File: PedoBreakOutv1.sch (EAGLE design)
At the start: 18 parts, among them IC1 LM1117MPX-2.85, J1 1050170001, J2 POWER_JACKSLT, J3 AVR_SPI_PROG_3X2NS, U1 ATTINY85-20P

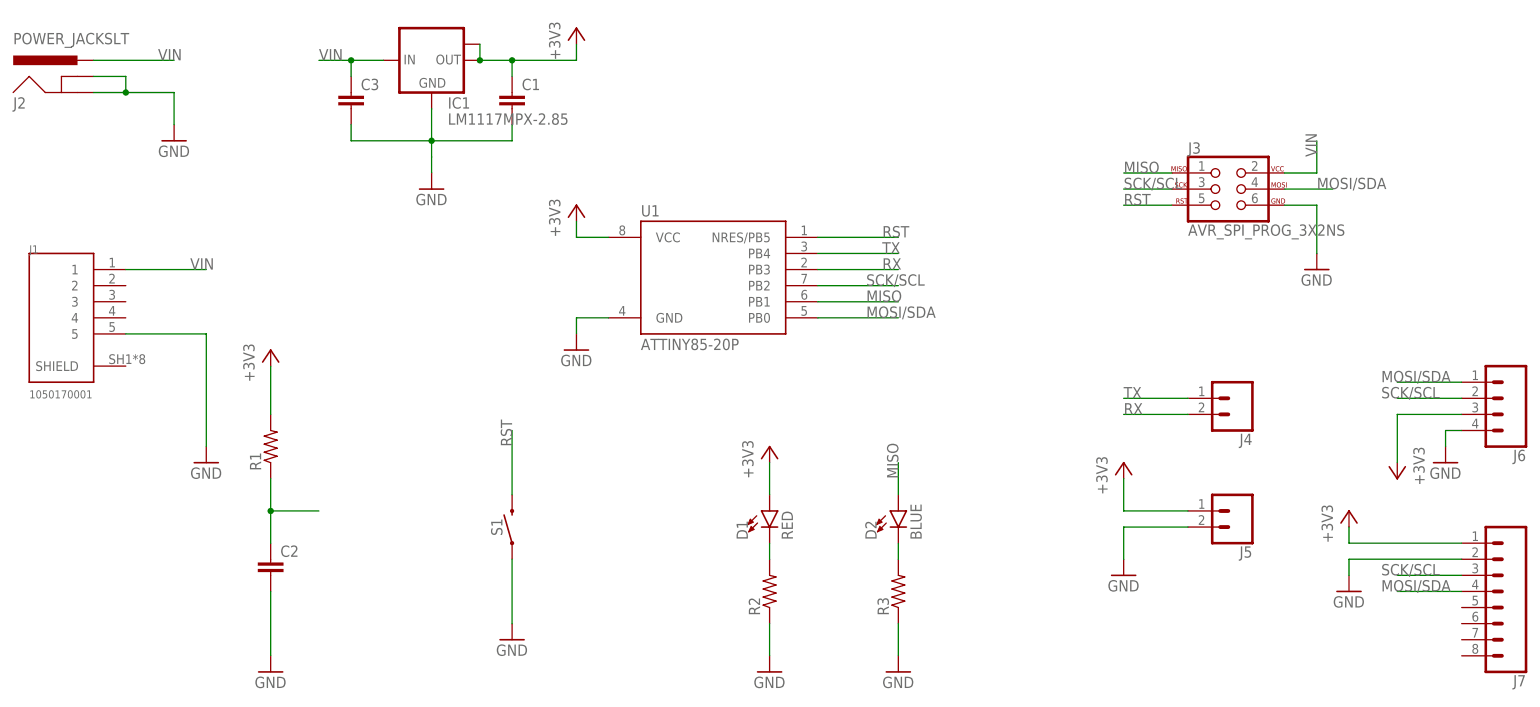
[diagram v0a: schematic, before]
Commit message: Reduced size of board, removed ground plane issues
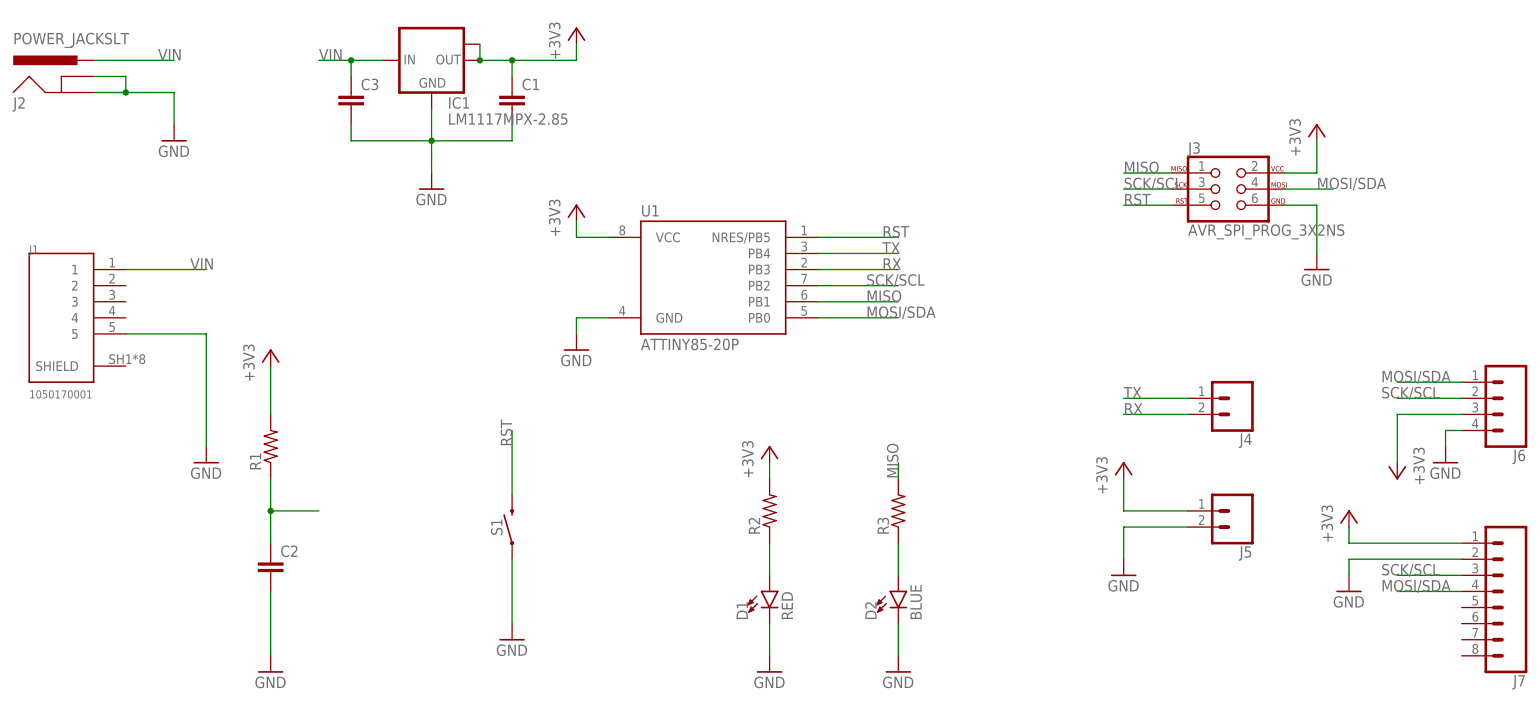
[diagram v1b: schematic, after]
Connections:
- net +3V3: now also J3.2, R2.2; no longer D1.A
- net GND: now also D1.C, D2.C; no longer R2.1, R3.1
- net MISO: now also R3.2; no longer D2.A
- net N$1: now also D1.A, R2.1; no longer D1.C, R2.2
- net N$3: now also D2.A, R3.1; no longer D2.C, R3.2
- net VIN: no longer J3.2
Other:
- moved on the sheet: D1, D2, R2, R3
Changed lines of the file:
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@@
 <?xml version="1.0" encoding="utf-8"?>
 <!DOCTYPE eagle SYSTEM "eagle.dtd">
-<eagle version="9.4.2">
+<eagle version="9.5.2">
 <drawing>
 <settings>
@@
 <part name="GND12" library="supply1" library_urn="urn:adsk.eagle:library:371" deviceset="GND" device=""/>
 <part name="IC1" library="lm1117" deviceset="LM1117MPX-*" device="" technology="2.85"/>
+<part name="+3V8" library="supply1" library_urn="urn:adsk.eagle:library:371" deviceset="+3V3" device=""/>
 </parts>
 <sheets>
@@
 <attribute name="VALUE" x="55.88" y="38.1" size="1.778" layer="96"/>
 </instance>
-<instance part="D1" gate="G$1" x="137.16" y="66.04" smashed="yes">
-<attribute name="NAME" x="133.731" y="61.468" size="1.778" layer="95" font="vector" rot="R90"/>
-<attribute name="VALUE" x="139.065" y="61.468" size="1.778" layer="96" font="vector" rot="R90" align="top-left"/>
-</instance>
-<instance part="D2" gate="G$1" x="157.48" y="66.04" smashed="yes">
-<attribute name="NAME" x="154.051" y="61.468" size="1.778" layer="95" font="vector" rot="R90"/>
-<attribute name="VALUE" x="159.385" y="61.468" size="1.778" layer="96" font="vector" rot="R90" align="top-left"/>
-</instance>
-<instance part="R2" gate="G$1" x="137.16" y="53.34" smashed="yes" rot="R90">
-<attribute name="NAME" x="135.6614" y="49.53" size="1.778" layer="95" rot="R90"/>
-<attribute name="VALUE" x="140.462" y="49.53" size="1.778" layer="96" rot="R90"/>
-</instance>
-<instance part="R3" gate="G$1" x="157.48" y="53.34" smashed="yes" rot="R90">
-<attribute name="NAME" x="155.9814" y="49.53" size="1.778" layer="95" rot="R90"/>
-<attribute name="VALUE" x="160.782" y="49.53" size="1.778" layer="96" rot="R90"/>
+<instance part="D1" gate="G$1" x="137.16" y="53.34" smashed="yes">
+<attribute name="NAME" x="133.731" y="48.768" size="1.778" layer="95" font="vector" rot="R90"/>
+<attribute name="VALUE" x="139.065" y="48.768" size="1.778" layer="96" font="vector" rot="R90" align="top-left"/>
+</instance>
+<instance part="D2" gate="G$1" x="157.48" y="53.34" smashed="yes">
+<attribute name="NAME" x="154.051" y="48.768" size="1.778" layer="95" font="vector" rot="R90"/>
+<attribute name="VALUE" x="159.385" y="48.768" size="1.778" layer="96" font="vector" rot="R90" align="top-left"/>
+</instance>
+<instance part="R2" gate="G$1" x="137.16" y="66.04" smashed="yes" rot="R90">
+<attribute name="NAME" x="135.6614" y="62.23" size="1.778" layer="95" rot="R90"/>
+<attribute name="VALUE" x="140.462" y="62.23" size="1.778" layer="96" rot="R90"/>
+</instance>
+<instance part="R3" gate="G$1" x="157.48" y="66.04" smashed="yes" rot="R90">
+<attribute name="NAME" x="155.9814" y="62.23" size="1.778" layer="95" rot="R90"/>
+<attribute name="VALUE" x="160.782" y="62.23" size="1.778" layer="96" rot="R90"/>
 </instance>
 <instance part="GND7" gate="1" x="137.16" y="40.64" smashed="yes">
@@
 <attribute name="NAME" x="86.36" y="129.54" size="1.778" layer="95"/>
 <attribute name="VALUE" x="86.36" y="127" size="1.778" layer="96"/>
+</instance>
+<instance part="+3V8" gate="G$1" x="223.52" y="127" smashed="yes">
+<attribute name="VALUE" x="220.98" y="121.92" size="1.778" layer="96" rot="R90"/>
 </instance>
 </instances>
@@
 </segment>
 <segment>
-<pinref part="R2" gate="G$1" pin="1"/>
-<pinref part="GND7" gate="1" pin="GND"/>
-<wire x1="137.16" y1="48.26" x2="137.16" y2="43.18" width="0.1524" layer="91"/>
-</segment>
-<segment>
-<pinref part="R3" gate="G$1" pin="1"/>
-<pinref part="GND8" gate="1" pin="GND"/>
-<wire x1="157.48" y1="48.26" x2="157.48" y2="43.18" width="0.1524" layer="91"/>
-</segment>
-<segment>
 <pinref part="J3" gate="G$1" pin="6"/>
 <wire x1="218.44" y1="114.3" x2="223.52" y2="114.3" width="0.1524" layer="91"/>
@@
 <pinref part="GND12" gate="1" pin="GND"/>
 <wire x1="228.6" y1="58.42" x2="228.6" y2="55.88" width="0.1524" layer="91"/>
+</segment>
+<segment>
+<pinref part="D1" gate="G$1" pin="C"/>
+<pinref part="GND7" gate="1" pin="GND"/>
+<wire x1="137.16" y1="48.26" x2="137.16" y2="43.18" width="0.1524" layer="91"/>
+</segment>
+<segment>
+<pinref part="D2" gate="G$1" pin="C"/>
+<pinref part="GND8" gate="1" pin="GND"/>
+<wire x1="157.48" y1="48.26" x2="157.48" y2="43.18" width="0.1524" layer="91"/>
 </segment>
 </net>
@@
 <wire x1="71.12" y1="137.16" x2="76.2" y2="137.16" width="0.1524" layer="91"/>
 <junction x="71.12" y="137.16"/>
-</segment>
-<segment>
-<pinref part="J3" gate="G$1" pin="2"/>
-<wire x1="218.44" y1="119.38" x2="223.52" y2="119.38" width="0.1524" layer="91"/>
-<wire x1="223.52" y1="119.38" x2="223.52" y2="124.46" width="0.1524" layer="91"/>
-<label x="223.52" y="121.92" size="1.778" layer="95" rot="R90"/>
 </segment>
 <segment>
@@
 </segment>
 <segment>
-<pinref part="D1" gate="G$1" pin="A"/>
-<wire x1="137.16" y1="68.58" x2="137.16" y2="73.66" width="0.1524" layer="91"/>
-<pinref part="+3V4" gate="G$1" pin="+3V3"/>
-</segment>
-<segment>
 <pinref part="J5" gate="G$1" pin="1"/>
 <wire x1="203.2" y1="66.04" x2="193.04" y2="66.04" width="0.1524" layer="91"/>
@@
 <pinref part="+3V2" gate="G$1" pin="+3V3"/>
 <wire x1="106.68" y1="109.22" x2="106.68" y2="111.76" width="0.1524" layer="91"/>
+</segment>
+<segment>
+<pinref part="+3V4" gate="G$1" pin="+3V3"/>
+<pinref part="R2" gate="G$1" pin="2"/>
+<wire x1="137.16" y1="73.66" x2="137.16" y2="71.12" width="0.1524" layer="91"/>
+</segment>
+<segment>
+<pinref part="+3V8" gate="G$1" pin="+3V3"/>
+<pinref part="J3" gate="G$1" pin="2"/>
+<wire x1="223.52" y1="124.46" x2="223.52" y2="119.38" width="0.1524" layer="91"/>
+<wire x1="223.52" y1="119.38" x2="218.44" y2="119.38" width="0.1524" layer="91"/>
 </segment>
 </net>
@@
 </segment>
 </net>
-<net name="N$1" class="0">
-<segment>
-<pinref part="D1" gate="G$1" pin="C"/>
-<pinref part="R2" gate="G$1" pin="2"/>
-<wire x1="137.16" y1="60.96" x2="137.16" y2="58.42" width="0.1524" layer="91"/>
-</segment>
-</net>
-<net name="N$3" class="0">
-<segment>
-<pinref part="D2" gate="G$1" pin="C"/>
-<pinref part="R3" gate="G$1" pin="2"/>
-<wire x1="157.48" y1="60.96" x2="157.48" y2="58.42" width="0.1524" layer="91"/>
-</segment>
-</net>
 <net name="MISO" class="0">
-<segment>
-<pinref part="D2" gate="G$1" pin="A"/>
-<wire x1="157.48" y1="68.58" x2="157.48" y2="73.66" width="0.1524" layer="91"/>
-<label x="157.48" y="71.12" size="1.778" layer="95" rot="R90"/>
-</segment>
 <segment>
 <pinref part="U1" gate="G$1" pin="PB1"/>
@@
 <label x="193.04" y="119.38" size="1.778" layer="95"/>
 </segment>
+<segment>
+<pinref part="R3" gate="G$1" pin="2"/>
+<wire x1="157.48" y1="71.12" x2="157.48" y2="73.66" width="0.1524" layer="91"/>
+<label x="157.48" y="71.12" size="1.778" layer="95" rot="R90"/>
+</segment>
 </net>
 <net name="MOSI/SDA" class="0">
@@
 </segment>
 </net>
+<net name="N$1" class="0">
+<segment>
+<pinref part="R2" gate="G$1" pin="1"/>
+<pinref part="D1" gate="G$1" pin="A"/>
+<wire x1="137.16" y1="60.96" x2="137.16" y2="55.88" width="0.1524" layer="91"/>
+</segment>
+</net>
+<net name="N$3" class="0">
+<segment>
+<pinref part="R3" gate="G$1" pin="1"/>
+<pinref part="D2" gate="G$1" pin="A"/>
+<wire x1="157.48" y1="60.96" x2="157.48" y2="55.88" width="0.1524" layer="91"/>
+</segment>
+</net>
